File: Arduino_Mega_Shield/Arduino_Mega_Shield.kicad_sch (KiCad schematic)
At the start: 29 parts, among them J1 Motor Driver Connector, J10 Conn_01x02, J11 Conn_01x02, J12 Conn_01x02, J13 Conn_01x02, J14 Conn_01x02, J2 Motor Driver Connector, J3 Conn_01x04, J4 Conn_01x04, J5 Conn_01x04, J6 Conn_01x04, J7 Motor Driver Connector, J8 Motor Driver Connector, J9 Conn_01x02

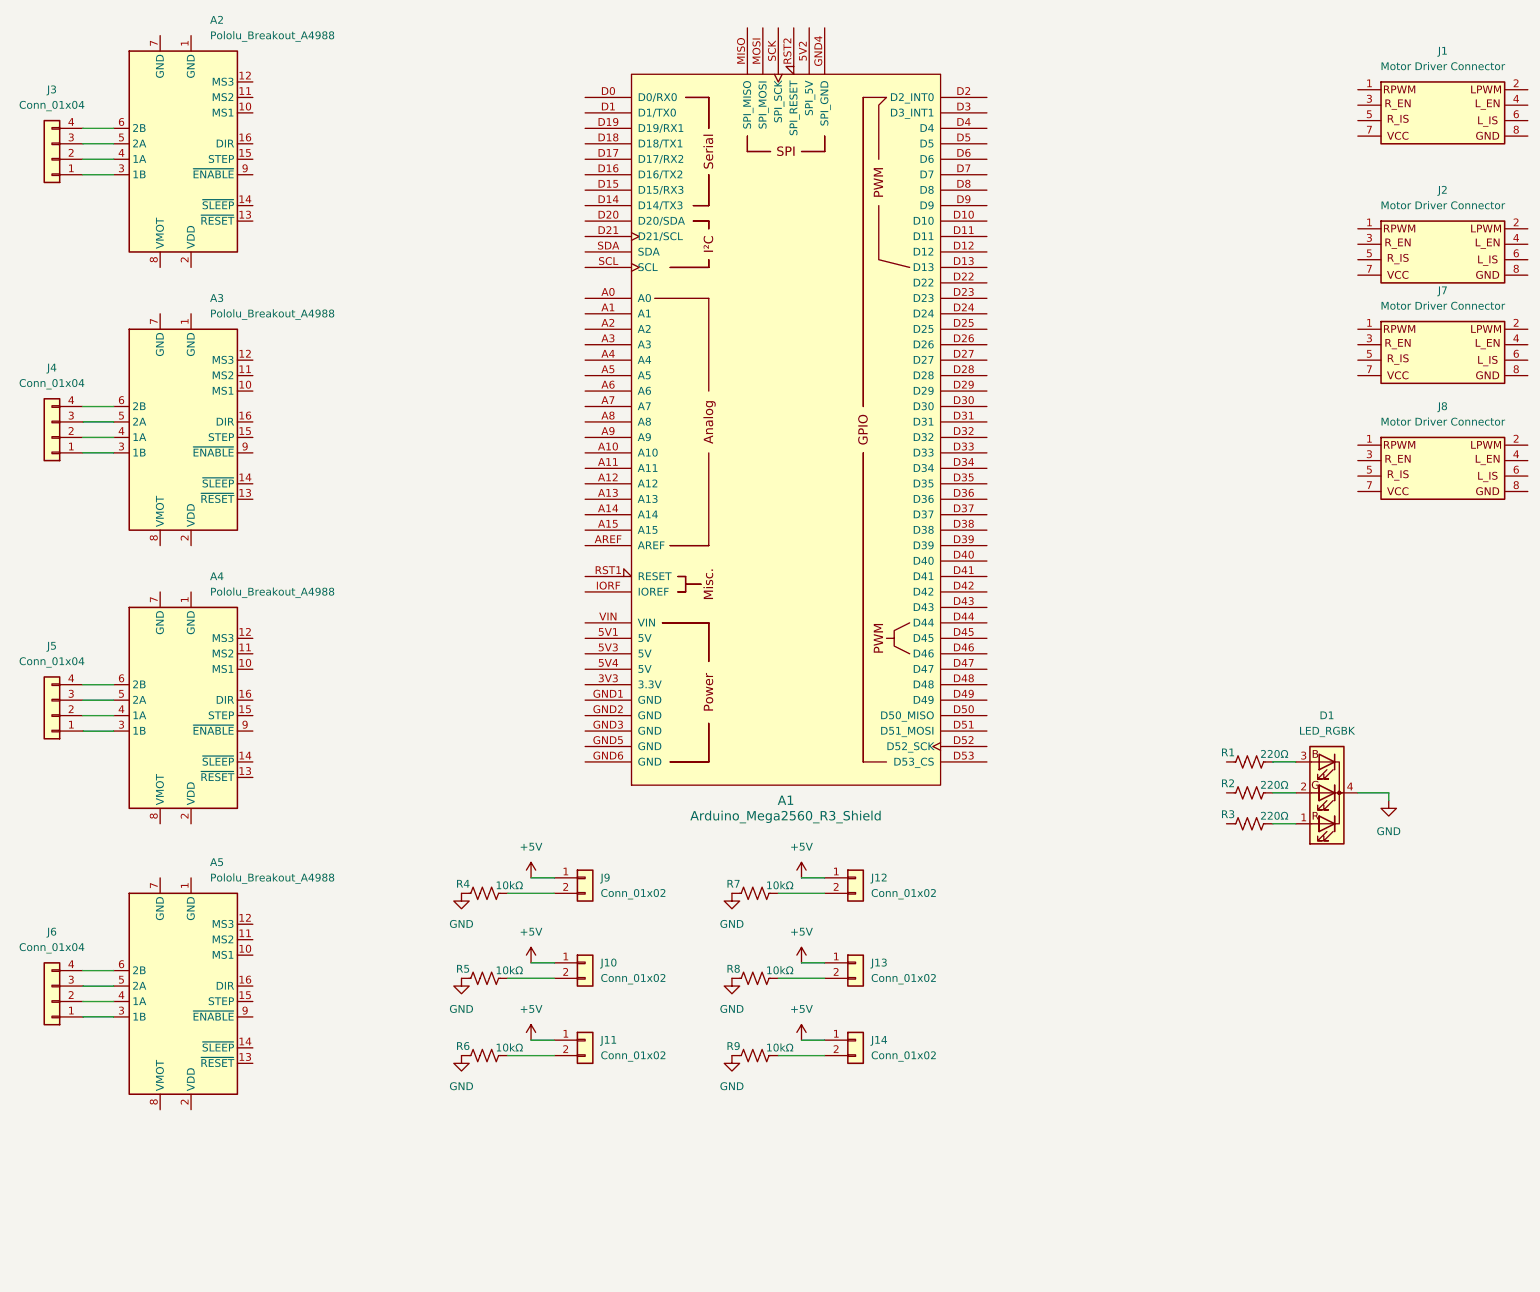
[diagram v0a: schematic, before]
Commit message: Update KiCad PCB (Pololu A4988) and ESP32 code
Replace Arduino Mega shield footprint with a Pololu A4988 breakout footprint and reorganize PCB item positions/annotations (silkscreen, fab, footprint properties, net index adjustments). Add several Arduino_Mega_Shield backup zip files. Also include changes to ESP-32 embedded code (src/main.cpp and src/motor_constants.hpp) — likely motor/driver-related updates to match the hardware footprint changes.
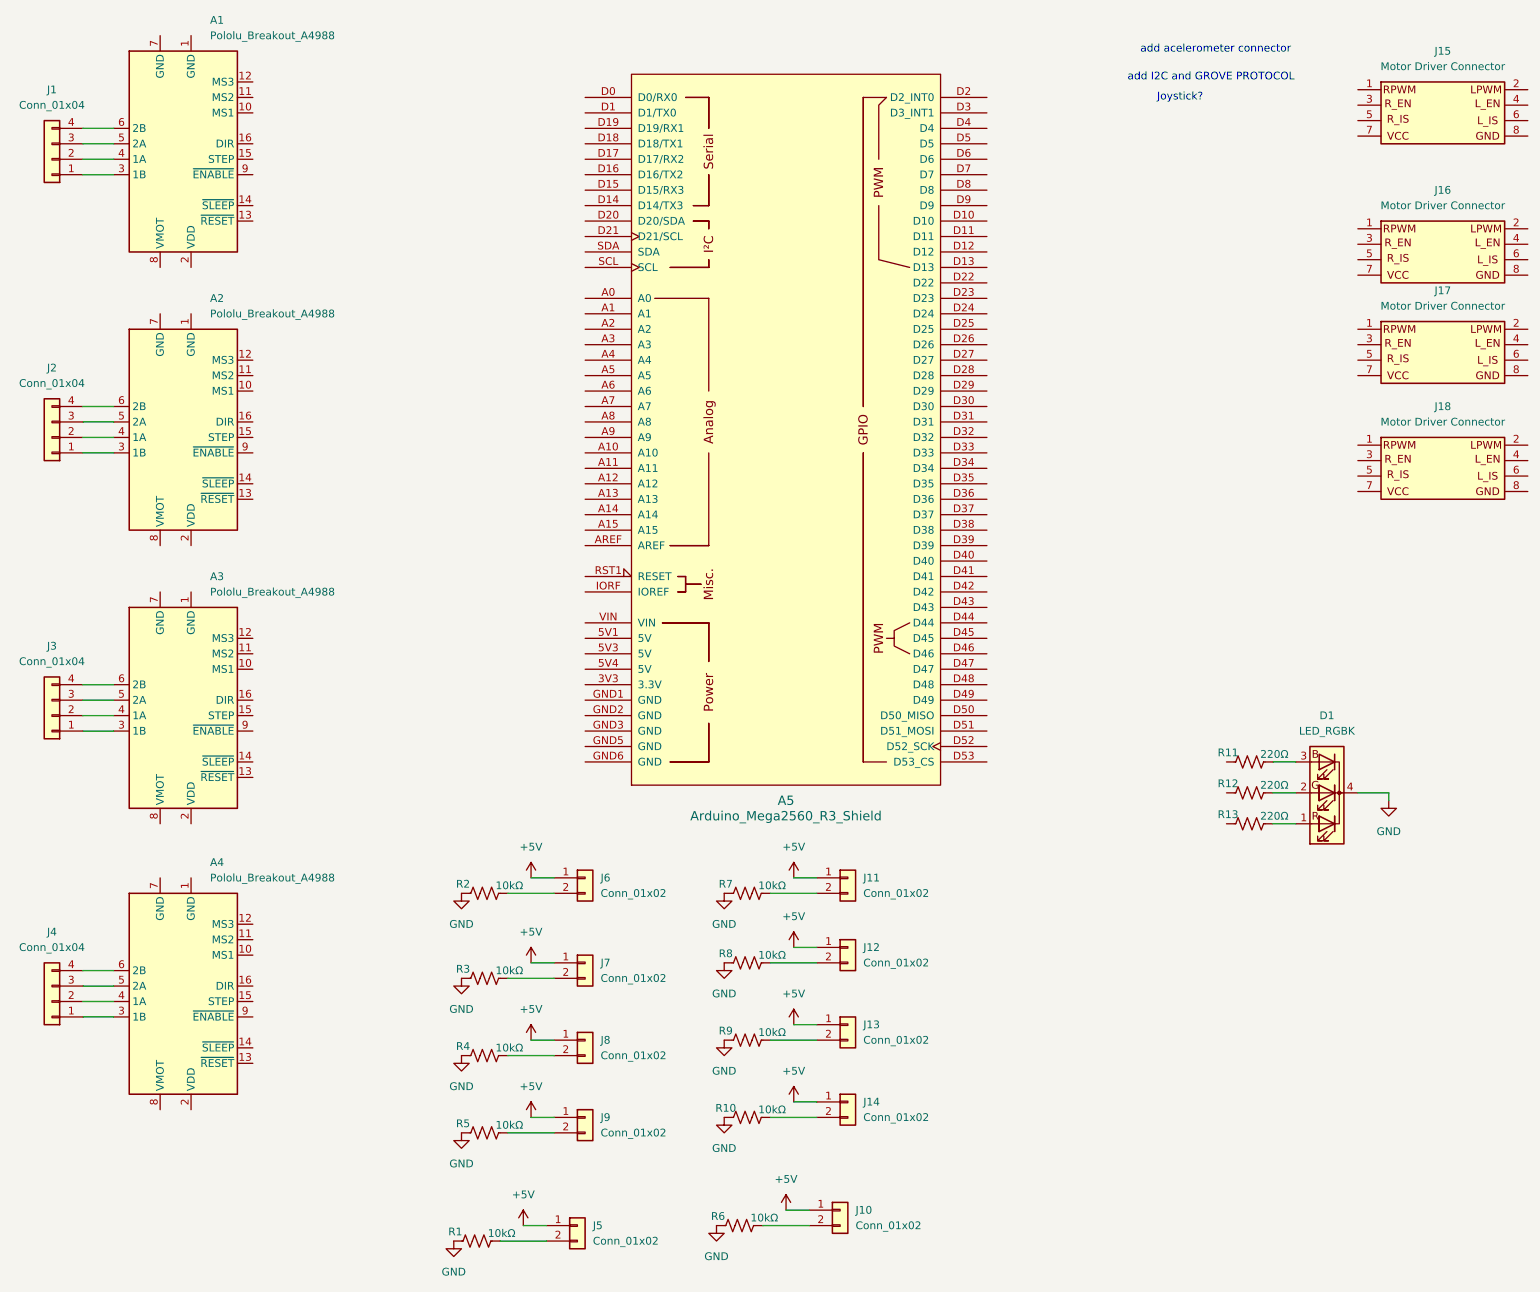
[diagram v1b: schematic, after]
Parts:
- added J10, J12, J13, J14: Conn_01x02, Connector_PinHeader_2.54mm:PinHeader_1x02_P2.54mm_Vertical, symbol Connector_Generic:Conn_01x02
- added R10, R6, R8, R9: 10kΩ, Resistor_THT:R_Axial_DIN0207_L6.3mm_D2.5mm_P7.62mm_Horizontal, symbol Device:R_US
- renumbered A2 to A1, A3 to A2, A4 to A3, A5 to A4, A1 to A5, J3 to J1, J14 to J11, J1 to J15, J2 to J16, J7 to J17, J8 to J18, J4 to J2, J5 to J3, J6 to J4, J13 to J5, J9 to J6, J10 to J7, J11 to J8, J12 to J9, R8 to R1, R1 to R11, R2 to R12, R3 to R13, R4 to R2, R5 to R3, R6 to R4, R7 to R5, R9 to R7
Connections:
- net +5V: now also J10.1 (Pin_1), J12.1 (Pin_1), J13.1 (Pin_1), J14.1 (Pin_1)
- net GND: now also R10.1, R6.1, R8.1, R9.1
- new net: J10.2 (Pin_2), R6.2
- new net: J13.2 (Pin_2), R9.2
- new net: J12.2 (Pin_2), R8.2
- new net: J14.2 (Pin_2), R10.2
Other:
- note added: "Joystick?"
- note added: "add I2C and GROVE PROTOCOL"
- note added: "add acelerometer connector"
- moved on the sheet: J11, J5, J9, R1, R5, R7

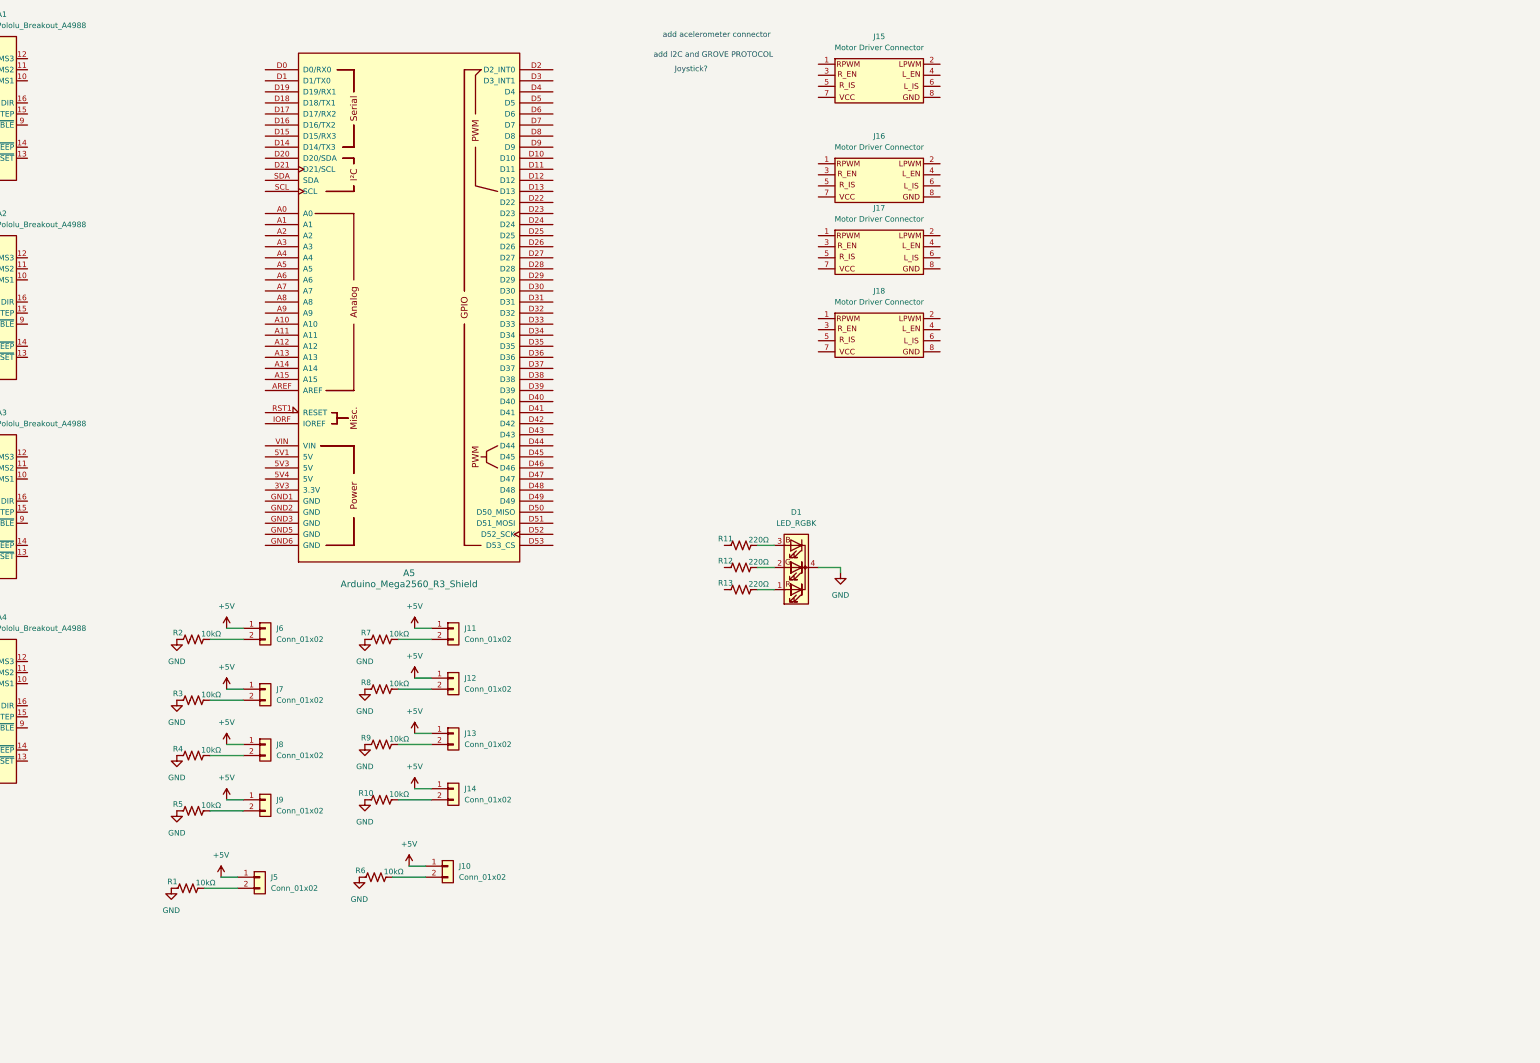
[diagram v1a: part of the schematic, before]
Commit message: Revise KiCad PCB footprints and add backups
Large update to the Arduino_Mega_Shield KiCad project: modified .kicad_pcb/.kicad_prl/.kicad_pro/.kicad_sch to replace and update connector footprints (JST XH, pin headers), adjust pad shapes/drills, 3D model refs, net names and UUIDs. Project housekeeping: removed autosave and lock files, renamed an autosave schematic to a .kicad_sch-bak, added multiple Arduino_Mega_Shield-backups ZIPs and added freerouting.rules. These changes consolidate footprint fixes and clean up temporary files prior to routing.
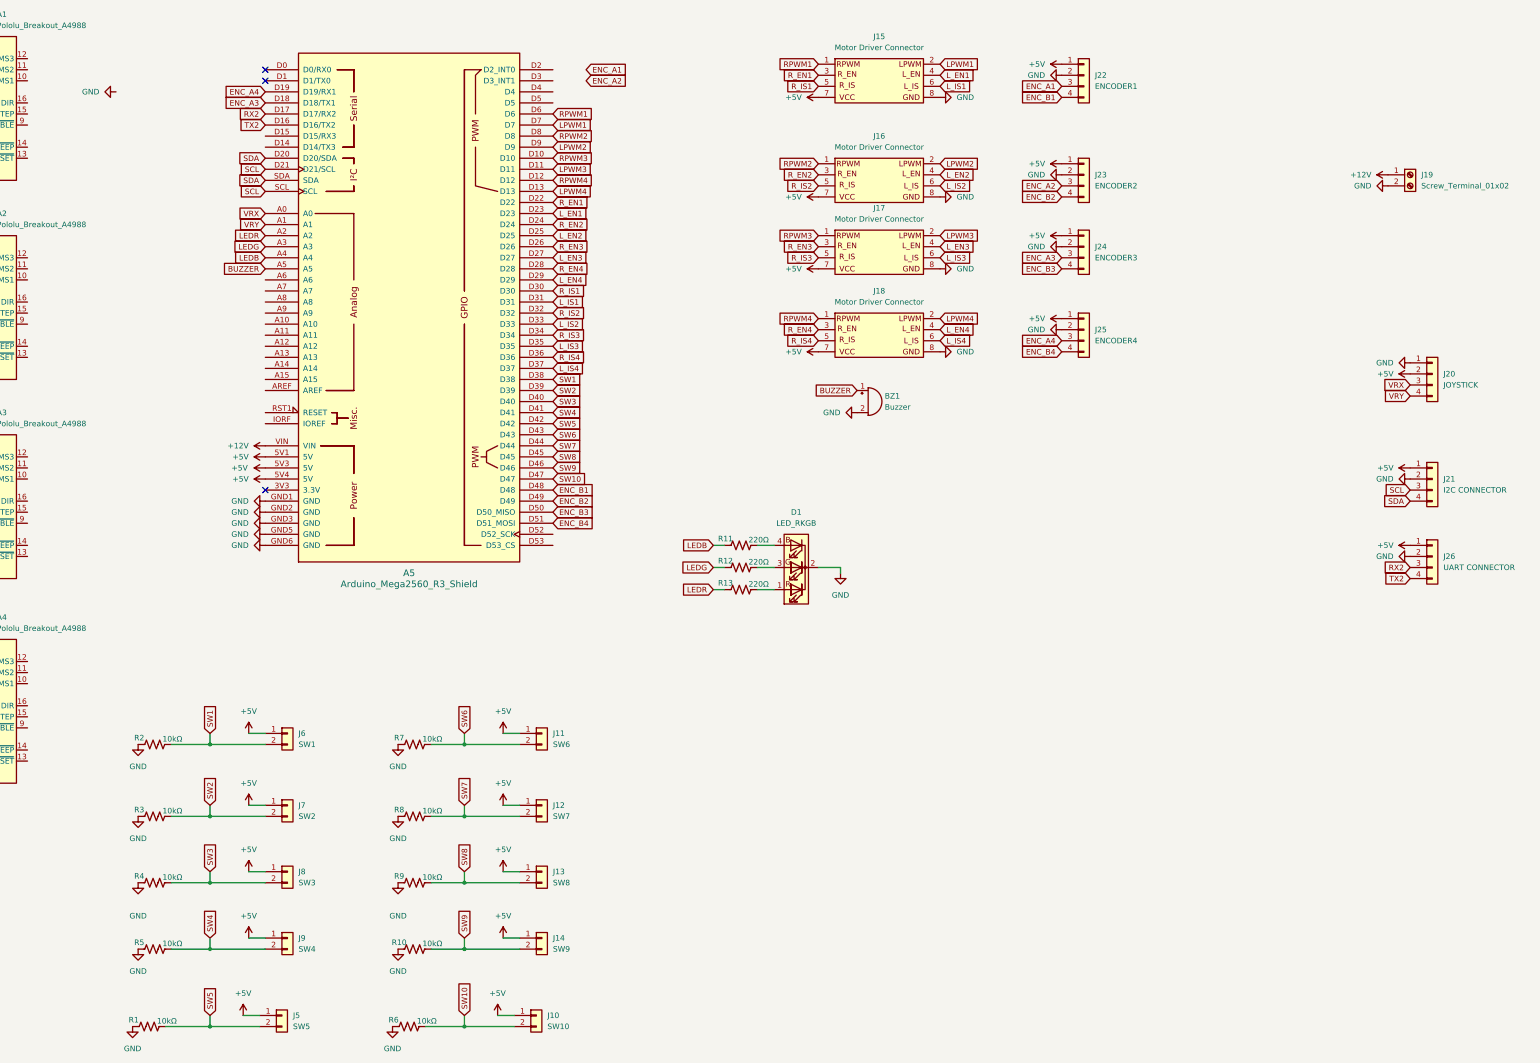
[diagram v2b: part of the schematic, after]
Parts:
- removed D1: LED_RGBK, LED_THT:LED_D5.0mm-4_RGB, symbol Device:LED_RGBK
- added BZ1: Buzzer, Buzzer_Beeper:Buzzer_12x9.5RM7.6, symbol Device:Buzzer
- added D1: LED_RKGB, LED_THT:LED_D5.0mm-4_RGB_Wide_Pins, symbol Device:LED_RKGB
- added J19: Screw_Terminal_01x02, TerminalBlock_RND:TerminalBlock_RND_205-00232_1x02_P5.08mm_Horizontal, symbol Connector:Screw_Terminal_01x02
- added J20: JOYSTICK, Connector_JST:JST_XH_B4B-XH-A_1x04_P2.50mm_Vertical, symbol Connector_Generic:Conn_01x04
- added J21: I2C CONNECTOR, Connector_JST:JST_XH_B4B-XH-A_1x04_P2.50mm_Vertical, symbol Connector_Generic:Conn_01x04
- added J22: ENCODER1, Connector_JST:JST_XH_B4B-XH-A_1x04_P2.50mm_Vertical, symbol Connector_Generic:Conn_01x04
- added J23: ENCODER2, Connector_JST:JST_XH_B4B-XH-A_1x04_P2.50mm_Vertical, symbol Connector_Generic:Conn_01x04
- added J24: ENCODER3, Connector_JST:JST_XH_B4B-XH-A_1x04_P2.50mm_Vertical, symbol Connector_Generic:Conn_01x04
- added J25: ENCODER4, Connector_JST:JST_XH_B4B-XH-A_1x04_P2.50mm_Vertical, symbol Connector_Generic:Conn_01x04
- added J26: UART CONNECTOR, Connector_JST:JST_XH_B4B-XH-A_1x04_P2.50mm_Vertical, symbol Connector_Generic:Conn_01x04
- J1, J2, J3, J4: footprint Connector_PinHeader_2.54mm:PinHeader_1x04_P2.54mm_Vertical -> Connector_JST:JST_XH_B4B-XH-A_1x04_P2.50mm_Vertical
- J10: value Conn_01x02 -> SW10
- J11: value Conn_01x02 -> SW6
- J12: value Conn_01x02 -> SW7
- J13: value Conn_01x02 -> SW8
- J14: value Conn_01x02 -> SW9
- J5: value Conn_01x02 -> SW5
- J6: value Conn_01x02 -> SW1
- J7: value Conn_01x02 -> SW2
- J8: value Conn_01x02 -> SW3
- J9: value Conn_01x02 -> SW4
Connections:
- net +5V: now also A5.5V1 (5V), A5.5V3 (5V), A5.5V4 (5V), J15.7 (Pin_7), J16.7 (Pin_7), J17.7 (Pin_7), J18.7 (Pin_7), J20.2 (Pin_2), J21.1 (Pin_1), J22.1 (Pin_1), J23.1 (Pin_1), J24.1 (Pin_1), J25.1 (Pin_1), J26.1 (Pin_1)
- net GND: now also A5.GND1 (GND), A5.GND2 (GND), A5.GND3 (GND), A5.GND5 (GND), A5.GND6 (GND), J15.8 (Pin_8), J16.8 (Pin_8), J17.8 (Pin_8), J18.8 (Pin_8), BZ1.2 (-), D1.2 (K), J19.2 (Pin_2), J20.1 (Pin_1), J21.2 (Pin_2), J22.2 (Pin_2), J23.2 (Pin_2), J24.2 (Pin_2), J25.2 (Pin_2), J26.2 (Pin_2)
- net SW1: now reaches J6.2 (Pin_2), R2.2
- net SW1: now also A5.D38
- net SW6: now reaches J11.2 (Pin_2), R7.2
- net SW6: now also A5.D43
- net SW2: now reaches J7.2 (Pin_2), R3.2
- net SW2: now also A5.D39
- net SW10: now reaches J10.2 (Pin_2), R6.2
- net SW10: now also A5.D47
- net SW5: now reaches J5.2 (Pin_2), R1.2
- net SW5: now also A5.D42
- net LEDG: now reaches R12.1
- net LEDG: now also A5.A3
- net at R12.2: now also D1.3 (GA)
- net LEDB: now reaches R11.1
- net LEDB: now also A5.A4
- net at R11.2: now also D1.4 (BA)
- net SW4: now reaches J9.2 (Pin_2), R5.2
- net SW4: now also A5.D41
- net SW3: now reaches J8.2 (Pin_2), R4.2
- net SW3: now also A5.D40
- net SW8: now reaches J13.2 (Pin_2), R9.2
- net SW8: now also A5.D45
- net RPWM1: now reaches J15.1 (Pin_1)
- net RPWM1: now also A5.D6
- net LPWM1: now reaches J15.2 (Pin_2)
- net LPWM1: now also A5.D7
- net R_EN1: now reaches J15.3 (Pin_3)
- net R_EN1: now also A5.D22
- net L_EN1: now reaches J15.4 (Pin_4)
- net L_EN1: now also A5.D23
- net R_IS1: now reaches J15.5 (Pin_5)
- net R_IS1: now also A5.D30
- net L_IS1: now reaches J15.6 (Pin_6)
- net L_IS1: now also A5.D31
- net SW7: now reaches J12.2 (Pin_2), R8.2
- net SW7: now also A5.D44
- net SW9: now reaches J14.2 (Pin_2), R10.2
- net SW9: now also A5.D46
- net at R13.2: now also D1.1 (RA)
- net RPWM4: now reaches J18.1 (Pin_1)
- net RPWM4: now also A5.D12
- net LPWM4: now reaches J18.2 (Pin_2)
- net LPWM4: now also A5.D13
- net R_EN4: now reaches J18.3 (Pin_3)
- net R_EN4: now also A5.D28
- net L_EN4: now reaches J18.4 (Pin_4)
- net L_EN4: now also A5.D29
- net R_IS4: now reaches J18.5 (Pin_5)
- net R_IS4: now also A5.D36
- net L_IS4: now reaches J18.6 (Pin_6)
- net L_IS4: now also A5.D37
- net VRX: now reaches A5.A0
- net VRX: now also J20.3 (Pin_3)
- net VRY: now reaches A5.A1
- net VRY: now also J20.4 (Pin_4)
- net LEDR: now reaches A5.A2
- net LEDR: now also R13.1
- net BUZZER: now reaches A5.A5
- net BUZZER: now also BZ1.1 (+)
- net RPWM3: now reaches A5.D10
- net RPWM3: now also J17.1 (Pin_1)
- net LPWM3: now reaches A5.D11
- net LPWM3: now also J17.2 (Pin_2)
- net TX2: now reaches A5.D16 (D16/TX2)
- net TX2: now also J26.4 (Pin_4)
- net RX2: now reaches A5.D17 (D17/RX2)
- net RX2: now also J26.3 (Pin_3)
- net ENC_A3: now reaches A5.D18 (D18/TX1)
- net ENC_A3: now also J24.3 (Pin_3)
- net ENC_A4: now reaches A5.D19 (D19/RX1)
- net ENC_A4: now also J25.3 (Pin_3)
- net SDA: now reaches A5.D20 (D20/SDA)
- net SDA: now also A5.SDA, J21.4 (Pin_4)
- net SCL: now reaches A5.D21 (D21/SCL)
- net SCL: now also A5.SCL, J21.3 (Pin_3)
- net R_EN2: now reaches A5.D24
- net R_EN2: now also J16.3 (Pin_3)
- net L_EN2: now reaches A5.D25
- net L_EN2: now also J16.4 (Pin_4)
- net R_EN3: now reaches A5.D26
- net R_EN3: now also J17.3 (Pin_3)
- net L_EN3: now reaches A5.D27
- net L_EN3: now also J17.4 (Pin_4)
- net R_IS2: now reaches A5.D32
- net R_IS2: now also J16.5 (Pin_5)
- net L_IS2: now reaches A5.D33
- net L_IS2: now also J16.6 (Pin_6)
- net R_IS3: now reaches A5.D34
- net R_IS3: now also J17.5 (Pin_5)
- net L_IS3: now reaches A5.D35
- net L_IS3: now also J17.6 (Pin_6)
- net ENC_B1: now reaches A5.D48
- net ENC_B1: now also J22.4 (Pin_4)
- net ENC_B2: now reaches A5.D49
- net ENC_B2: now also J23.4 (Pin_4)
- net ENC_B3: now reaches A5.D50 (D50_MISO)
- net ENC_B3: now also J24.4 (Pin_4)
- net ENC_B4: now reaches A5.D51 (D51_MOSI)
- net ENC_B4: now also J25.4 (Pin_4)
- net RPWM2: now reaches A5.D8
- net RPWM2: now also J16.1 (Pin_1)
- net LPWM2: now reaches A5.D9
- net LPWM2: now also J16.2 (Pin_2)
- net +12V: now reaches A5.VIN
- net +12V: now also J19.1 (Pin_1)
- new net ENC_A1: J22.3 (Pin_3)
- new net ENC_A2: J23.3 (Pin_3)
- no-connect marks 0 -> 3
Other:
- note removed: "Joystick?"
- note removed: "add I2C and GROVE PROTOCOL"
- note removed: "add acelerometer connector"
- moved on the sheet: J10, J11, J12, J13, J14, J5, J6, J7, J8, J9, R1, R10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
